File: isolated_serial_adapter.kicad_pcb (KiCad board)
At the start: 4 copper layers, 110 x 57 mm, 106 parts, among them J1 USB_C_Receptacle_USB2.0, J2 RS485_1, J3 TERM, J4 TERM, J5 RS485_2, J6 RS232_1, J7 RS232_1_FLOW, J8 UART_1, J9 UART_1_FLOW, SW1 RESET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

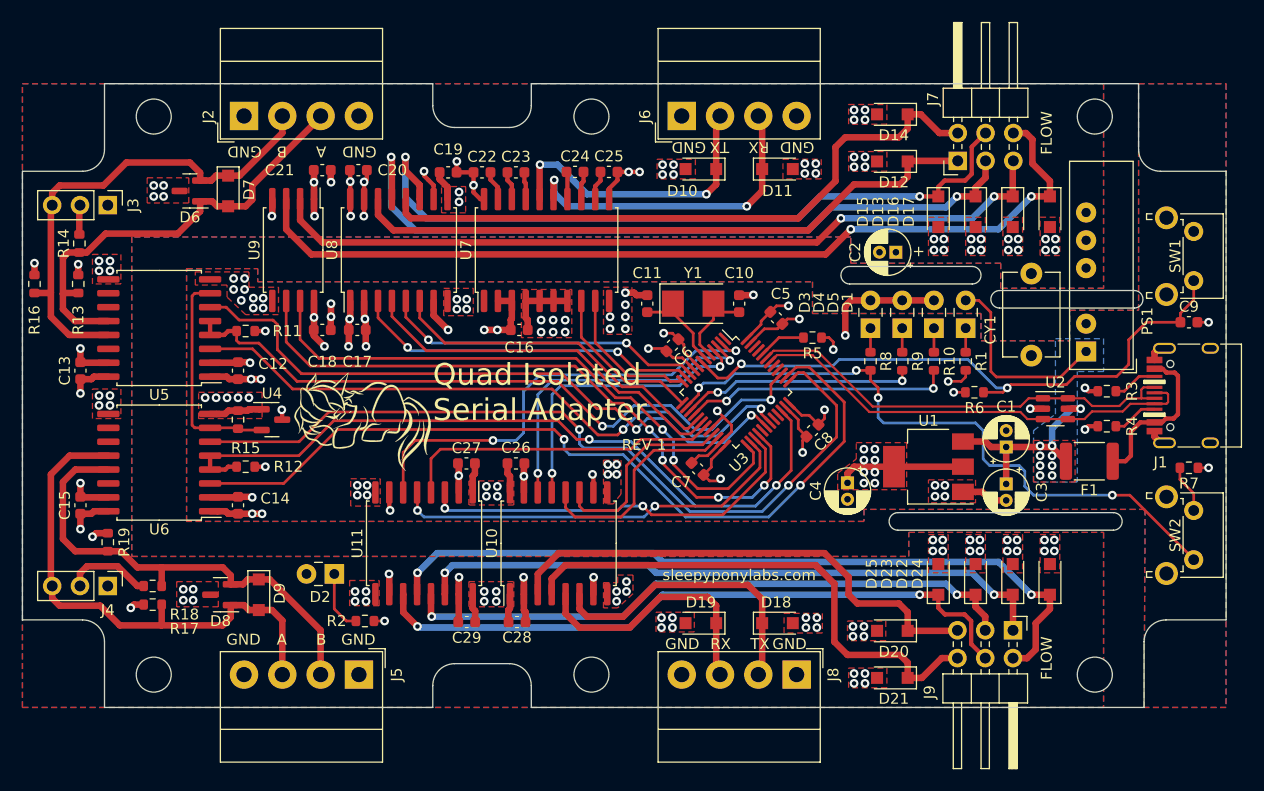
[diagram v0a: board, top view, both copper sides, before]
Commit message: Fix incorrect standoff clearances
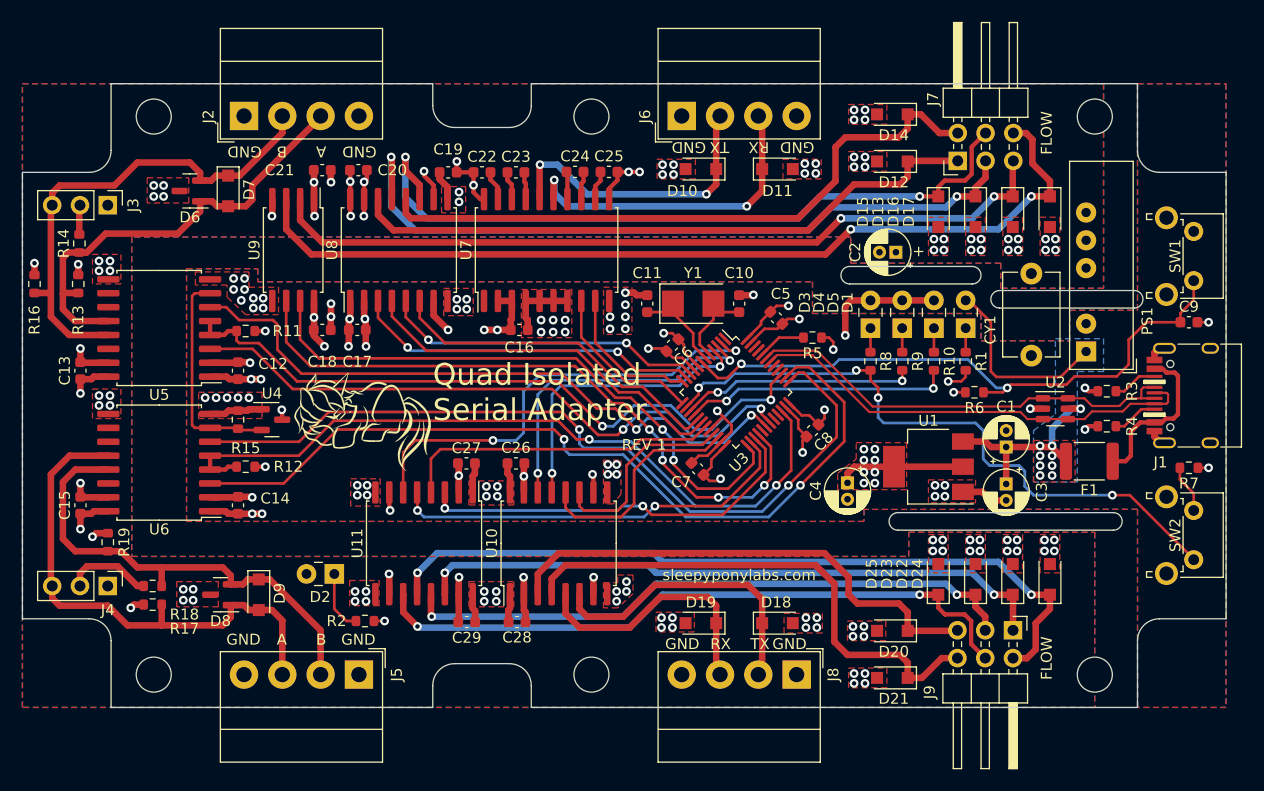
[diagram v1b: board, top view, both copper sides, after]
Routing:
- net VBUS: track 37.7 -> 37.1 mm
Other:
- outline, holes or cut-outs redrawn

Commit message: Fix NPTH and edge milling dimensions
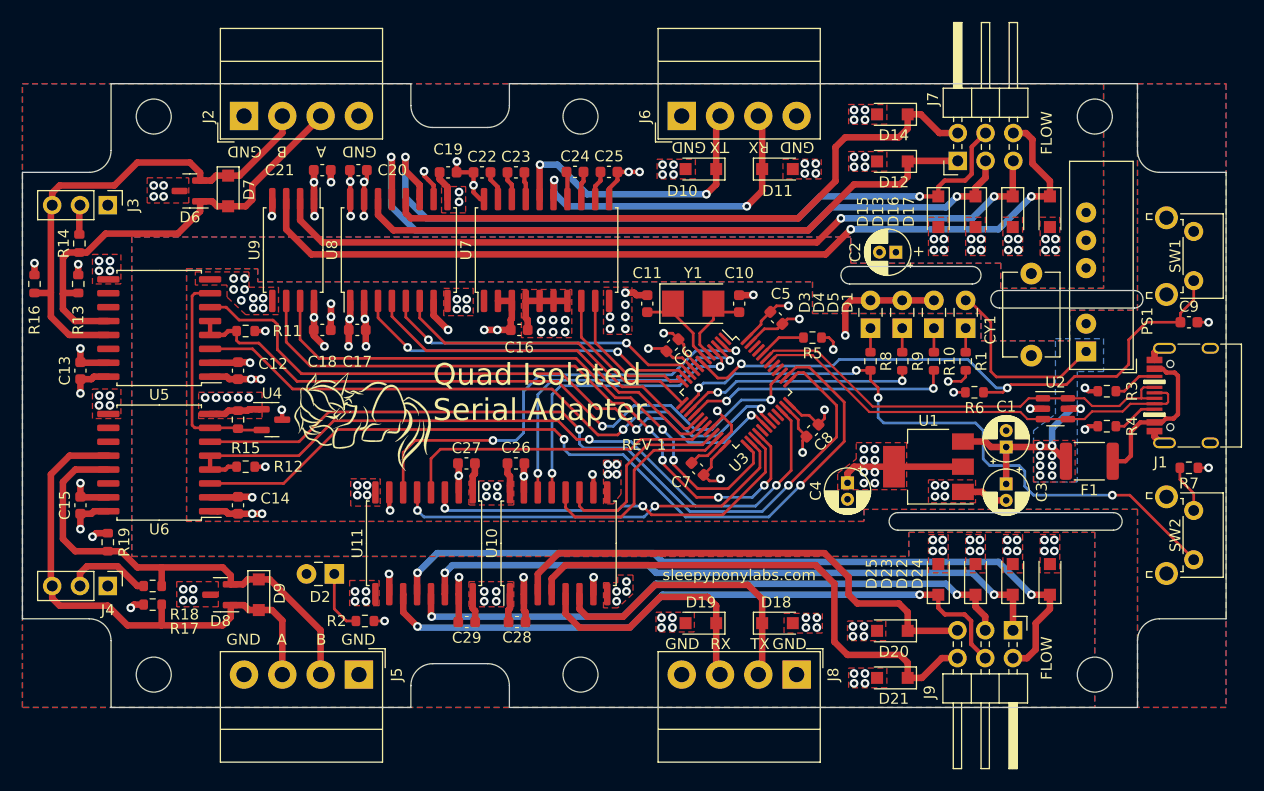
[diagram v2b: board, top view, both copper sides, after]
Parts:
- moved H2 1.00 mm to (131.0, 43.0)
- moved H5 1.00 mm to (131.0, 94.0)
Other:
- outline, holes or cut-outs redrawn
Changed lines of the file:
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@@
   )
   (footprint "MountingHole:MountingHole_3.2mm_M3" (layer "F.Cu")
-    (at 132 94)
+    (at 131 94)
     (descr "Mounting Hole 3.2mm, no annular, M3")
     (tags "mounting hole 3.2mm no annular m3")
@@
   )
   (footprint "MountingHole:MountingHole_3.2mm_M3" (layer "F.Cu")
-    (at 132 43)
+    (at 131 43)
     (descr "Mounting Hole 3.2mm, no annular, M3")
     (tags "mounting hole 3.2mm no annular m3")
@@
   (gr_arc (start 160 80.8) (mid 159.2 80) (end 160 79.2) (layer "Edge.Cuts") (width 0.1))
   (gr_line (start 155.6 56.7) (end 166.8 56.7) (layer "Edge.Cuts") (width 0.1))
-  (gr_line (start 181.9 97) (end 126.5 97) (layer "Edge.Cuts") (width 0.1))
-  (gr_line (start 117.5 40) (end 88.1 40) (layer "Edge.Cuts") (width 0.1))
+  (gr_line (start 181.9 97) (end 124.5 97) (layer "Edge.Cuts") (width 0.1))
+  (gr_line (start 115.5 40) (end 88.1 40) (layer "Edge.Cuts") (width 0.1))
   (gr_line (start 80 88.9) (end 80 48.1) (layer "Edge.Cuts") (width 0.1))
   (gr_line (start 190 48.1) (end 190 88.9) (layer "Edge.Cuts") (width 0.1))
-  (gr_line (start 117.5 40) (end 117.5 42) (layer "Edge.Cuts") (width 0.1))
+  (gr_line (start 115.5 40) (end 115.5 42) (layer "Edge.Cuts") (width 0.1))
   (gr_line (start 169.3 58.9) (end 181.6 58.9) (layer "Edge.Cuts") (width 0.1))
-  (gr_line (start 88.1 97) (end 117.5 97) (layer "Edge.Cuts") (width 0.1))
-  (gr_line (start 119.5 44) (end 124.5 44) (layer "Edge.Cuts") (width 0.1))
-  (gr_arc (start 119.5 44) (mid 118.085786 43.414214) (end 117.5 42) (layer "Edge.Cuts") (width 0.1))
+  (gr_line (start 88.1 97) (end 115.5 97) (layer "Edge.Cuts") (width 0.1))
+  (gr_line (start 117.5 44) (end 122.5 44) (layer "Edge.Cuts") (width 0.1))
+  (gr_arc (start 117.5 44) (mid 116.085786 43.414214) (end 115.5 42) (layer "Edge.Cuts") (width 0.1))
   (gr_arc (start 166.8 56.7) (mid 167.6 57.5) (end 166.8 58.3) (layer "Edge.Cuts") (width 0.1))
-  (gr_arc (start 124.5 93) (mid 125.914214 93.585786) (end 126.5 95) (layer "Edge.Cuts") (width 0.1))
+  (gr_arc (start 122.5 93) (mid 123.914214 93.585786) (end 124.5 95) (layer "Edge.Cuts") (width 0.1))
   (gr_arc (start 181.9 90.9) (mid 182.485786 89.485786) (end 183.9 88.9) (layer "Edge.Cuts") (width 0.1))
   (gr_line (start 155.6 58.3) (end 166.8 58.3) (layer "Edge.Cuts") (width 0.1))
-  (gr_arc (start 117.5 95) (mid 118.085786 93.585786) (end 119.5 93) (layer "Edge.Cuts") (width 0.1))
+  (gr_arc (start 115.5 95) (mid 116.085786 93.585786) (end 117.5 93) (layer "Edge.Cuts") (width 0.1))
   (gr_arc (start 183.9 48.1) (mid 182.485786 47.514214) (end 181.9 46.1) (layer "Edge.Cuts") (width 0.1))
-  (gr_line (start 126.5 40) (end 181.9 40) (layer "Edge.Cuts") (width 0.1))
+  (gr_line (start 124.5 40) (end 181.9 40) (layer "Edge.Cuts") (width 0.1))
   (gr_arc (start 179.7 79.2) (mid 180.5 80) (end 179.7 80.8) (layer "Edge.Cuts") (width 0.1))
   (gr_line (start 160 79.2) (end 179.7 79.2) (layer "Edge.Cuts") (width 0.1))
@@
   (gr_line (start 183.9 48.1) (end 190 48.1) (layer "Edge.Cuts") (width 0.1))
   (gr_line (start 181.9 40) (end 181.9 46.1) (layer "Edge.Cuts") (width 0.1))
-  (gr_line (start 126.5 42) (end 126.5 40) (layer "Edge.Cuts") (width 0.1))
-  (gr_line (start 119.5 93) (end 124.5 93) (layer "Edge.Cuts") (width 0.1))
+  (gr_line (start 124.5 42) (end 124.5 40) (layer "Edge.Cuts") (width 0.1))
+  (gr_line (start 117.5 93) (end 122.5 93) (layer "Edge.Cuts") (width 0.1))
   (gr_line (start 160 80.8) (end 179.7 80.8) (layer "Edge.Cuts") (width 0.1))
   (gr_line (start 181.9 97) (end 181.9 90.9) (layer "Edge.Cuts") (width 0.1))
   (gr_line (start 88.1 40) (end 88.1 46.1) (layer "Edge.Cuts") (width 0.1))
-  (gr_arc (start 126.5 42) (mid 125.914214 43.414214) (end 124.5 44) (layer "Edge.Cuts") (width 0.1))
+  (gr_arc (start 124.5 42) (mid 123.914214 43.414214) (end 122.5 44) (layer "Edge.Cuts") (width 0.1))
   (gr_line (start 86.1 48.1) (end 80 48.1) (layer "Edge.Cuts") (width 0.1))
-  (gr_line (start 117.5 97) (end 117.5 95) (layer "Edge.Cuts") (width 0.1))
+  (gr_line (start 115.5 97) (end 115.5 95) (layer "Edge.Cuts") (width 0.1))
   (gr_arc (start 88.1 46.1) (mid 87.514214 47.514214) (end 86.1 48.1) (layer "Edge.Cuts") (width 0.1))
-  (gr_line (start 126.5 95) (end 126.5 97) (layer "Edge.Cuts") (width 0.1))
+  (gr_line (start 124.5 95) (end 124.5 97) (layer "Edge.Cuts") (width 0.1))
   (gr_line (start 183.9 88.9) (end 190 88.9) (layer "Edge.Cuts") (width 0.1))
   (gr_arc (start 169.3 60.5) (mid 168.5 59.7) (end 169.3 58.9) (layer "Edge.Cuts") (width 0.1))
@@
   (gr_line (start 194 101) (end 76 101) (layer "User.2") (width 0.15))
   (gr_line (start 76 101) (end 76 36) (layer "User.2") (width 0.15))
-  (gr_line (start 123.5 95) (end 123.5 98) (layer "User.4") (width 0.15))
-  (gr_line (start 121.5 95) (end 119.5 95) (layer "User.4") (width 0.15))
+  (gr_line (start 121.5 95) (end 121.5 98) (layer "User.4") (width 0.15))
+  (gr_line (start 119.5 95) (end 117.5 95) (layer "User.4") (width 0.15))
   (gr_circle (center 84 44) (end 87.5 44) (layer "User.4") (width 0.15) (fill none))
-  (gr_line (start 124.5 98) (end 124.5 95) (layer "User.4") (width 0.15))
+  (gr_line (start 122.5 98) (end 122.5 95) (layer "User.4") (width 0.15))
   (gr_circle (center 84 44) (end 86.5 44) (layer "User.4") (width 0.15) (fill none))
-  (gr_line (start 121.5 39) (end 121.5 42) (layer "User.4") (width 0.15))
-  (gr_circle (center 132 43) (end 132 40.5) (layer "User.4") (width 0.15) (fill none))
-  (gr_line (start 123.5 42) (end 123.5 39) (layer "User.4") (width 0.15))
-  (gr_line (start 121.5 98) (end 121.5 95) (layer "User.4") (width 0.15))
+  (gr_line (start 119.5 39) (end 119.5 42) (layer "User.4") (width 0.15))
+  (gr_circle (center 131 43) (end 133.5 43) (layer "User.4") (width 0.15) (fill none))
+  (gr_line (start 121.5 42) (end 121.5 39) (layer "User.4") (width 0.15))
+  (gr_line (start 119.5 98) (end 119.5 95) (layer "User.4") (width 0.15))
   (gr_line (start 191 39) (end 191 98) (layer "User.4") (width 0.15))
   (gr_line (start 191 98) (end 79 98) (layer "User.4") (width 0.15))
   (gr_circle (center 186 93) (end 182.5 93) (layer "User.4") (width 0.15) (fill none))
-  (gr_line (start 121.5 42) (end 119.5 42) (layer "User.4") (width 0.15))
+  (gr_line (start 119.5 42) (end 117.5 42) (layer "User.4") (width 0.15))
   (gr_circle (center 186 93) (end 188.5 93) (layer "User.4") (width 0.15) (fill none))
   (gr_circle (center 178 43) (end 178 40.5) (layer "User.4") (width 0.15) (fill none))
@@
   (gr_circle (center 84 93) (end 87.5 93) (layer "User.4") (width 0.15) (fill none))
   (gr_circle (center 186 44) (end 182.5 44) (layer "User.4") (width 0.15) (fill none))
-  (gr_line (start 119.5 95) (end 119.5 98) (layer "User.4") (width 0.15))
+  (gr_line (start 117.5 95) (end 117.5 98) (layer "User.4") (width 0.15))
   (gr_line (start 79 39) (end 191 39) (layer "User.4") (width 0.15))
   (gr_line (start 79 98) (end 79 39) (layer "User.4") (width 0.15))
-  (gr_line (start 124.5 95) (end 123.5 95) (layer "User.4") (width 0.15))
+  (gr_line (start 122.5 95) (end 121.5 95) (layer "User.4") (width 0.15))
   (gr_circle (center 84 93) (end 86.5 93) (layer "User.4") (width 0.15) (fill none))
-  (gr_line (start 119.5 42) (end 119.5 39) (layer "User.4") (width 0.15))
-  (gr_circle (center 132 94) (end 132 91.5) (layer "User.4") (width 0.15) (fill none))
-  (gr_line (start 124.5 42) (end 123.5 42) (layer "User.4") (width 0.15))
-  (gr_line (start 124.5 39) (end 124.5 42) (layer "User.4") (width 0.15))
+  (gr_line (start 117.5 42) (end 117.5 39) (layer "User.4") (width 0.15))
+  (gr_circle (center 131 94) (end 133.5 94) (layer "User.4") (width 0.15) (fill none))
+  (gr_line (start 122.5 42) (end 121.5 42) (layer "User.4") (width 0.15))
+  (gr_line (start 122.5 39) (end 122.5 42) (layer "User.4") (width 0.15))
   (gr_circle (center 186 44) (end 188.5 44) (layer "User.4") (width 0.15) (fill none))
   (gr_text "SERIAL-1" (at 145.5 45.6) (layer "B.SilkS")
